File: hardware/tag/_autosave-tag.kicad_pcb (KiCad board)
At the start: 2 copper layers, 50 x 52 mm, 109 parts, among them J1 USB_C_Receptacle_USB2.0_16P, J2 BATTERY, J3 UART, J4 I2C, J5 STM SWD, J6 ADC, J7 BLE SWD, J8 SOURCE, SW1 RESET, SW2 BOOT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

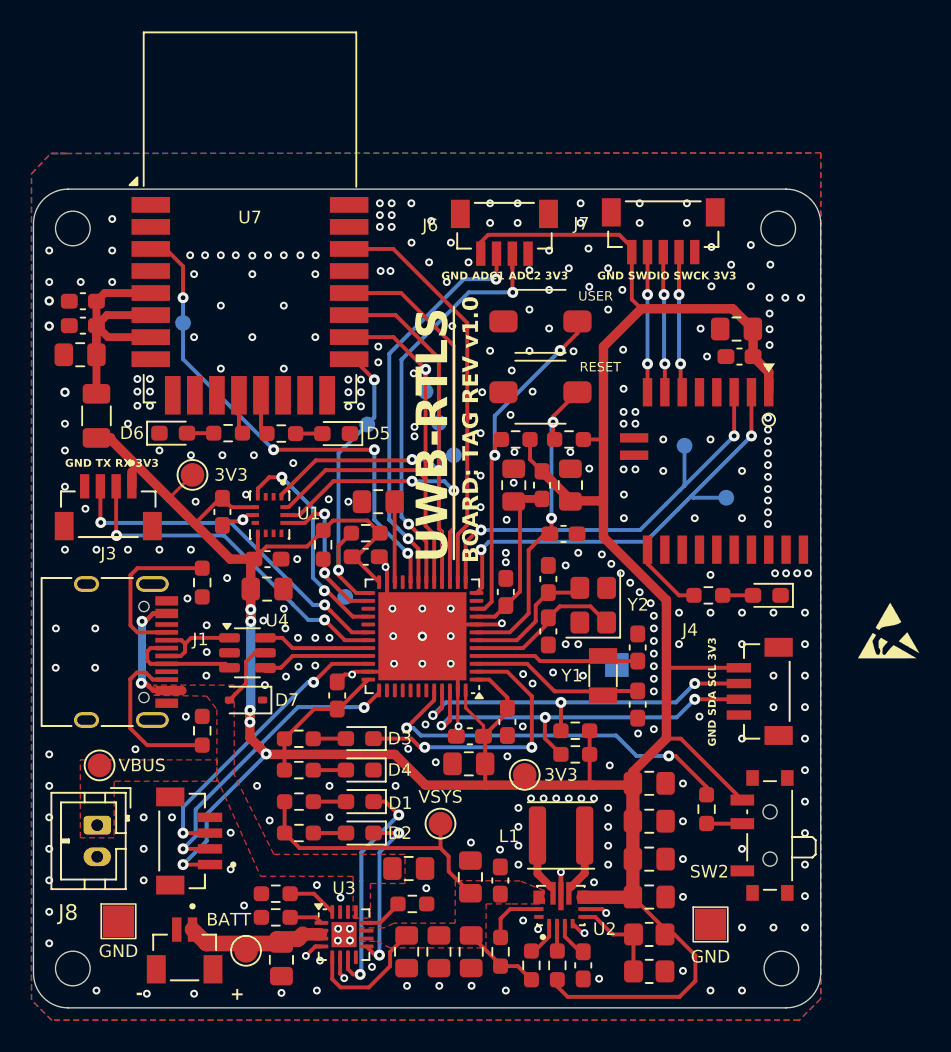
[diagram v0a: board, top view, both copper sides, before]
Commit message: feat(hardware): Save tag schematic & pcb layout
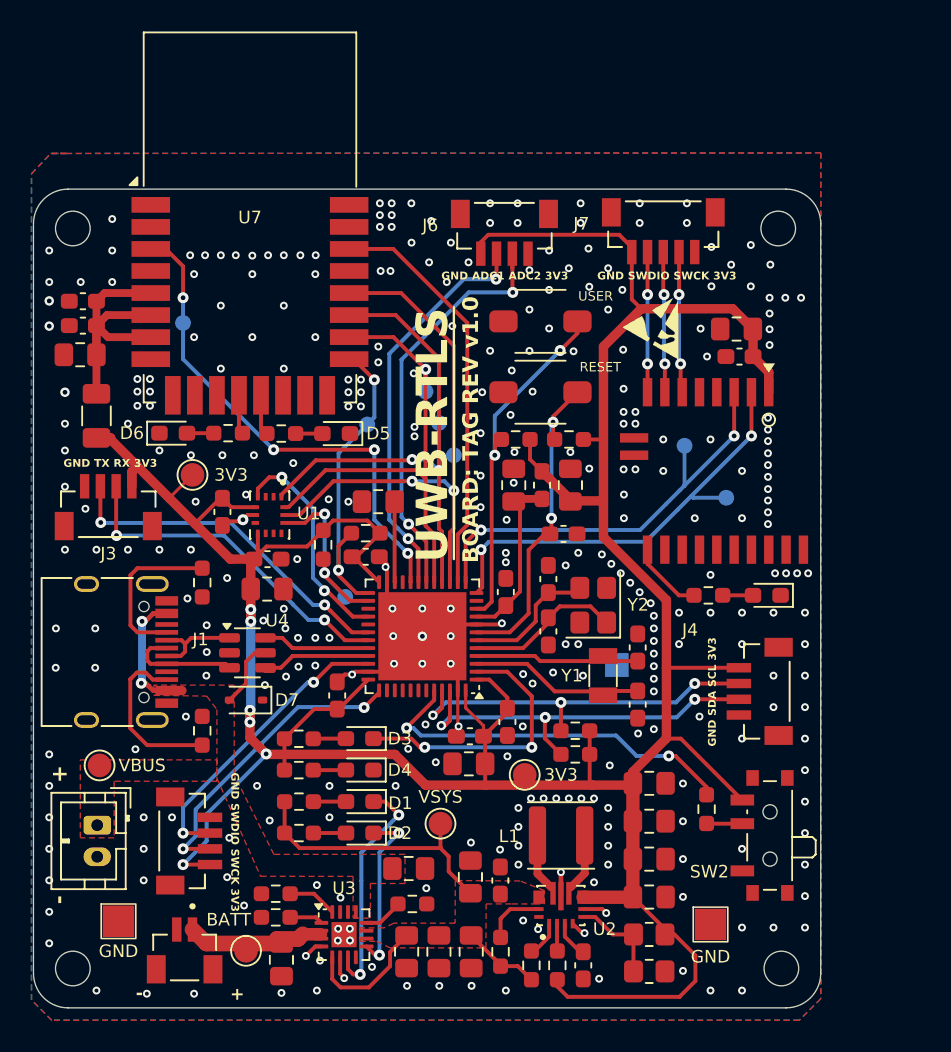
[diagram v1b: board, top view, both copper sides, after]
